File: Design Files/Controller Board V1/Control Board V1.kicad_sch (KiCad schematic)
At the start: 0 parts

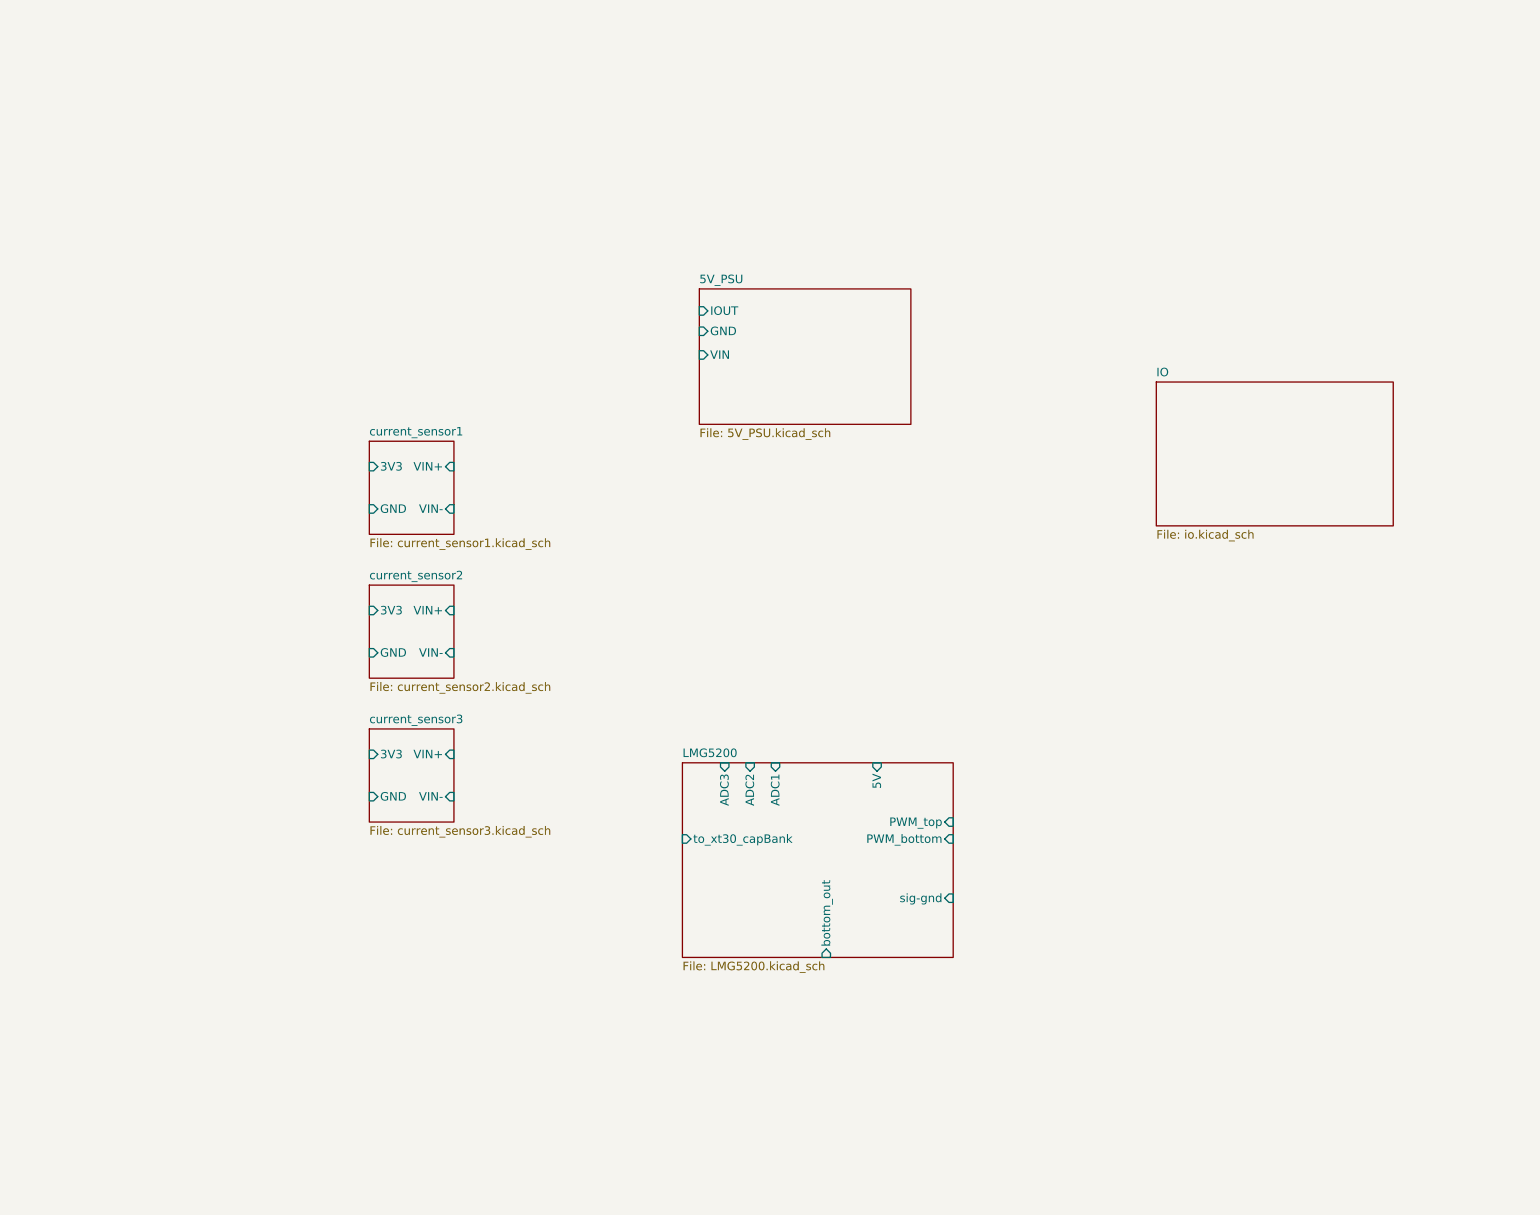
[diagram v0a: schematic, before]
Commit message: Pico Schematic Started
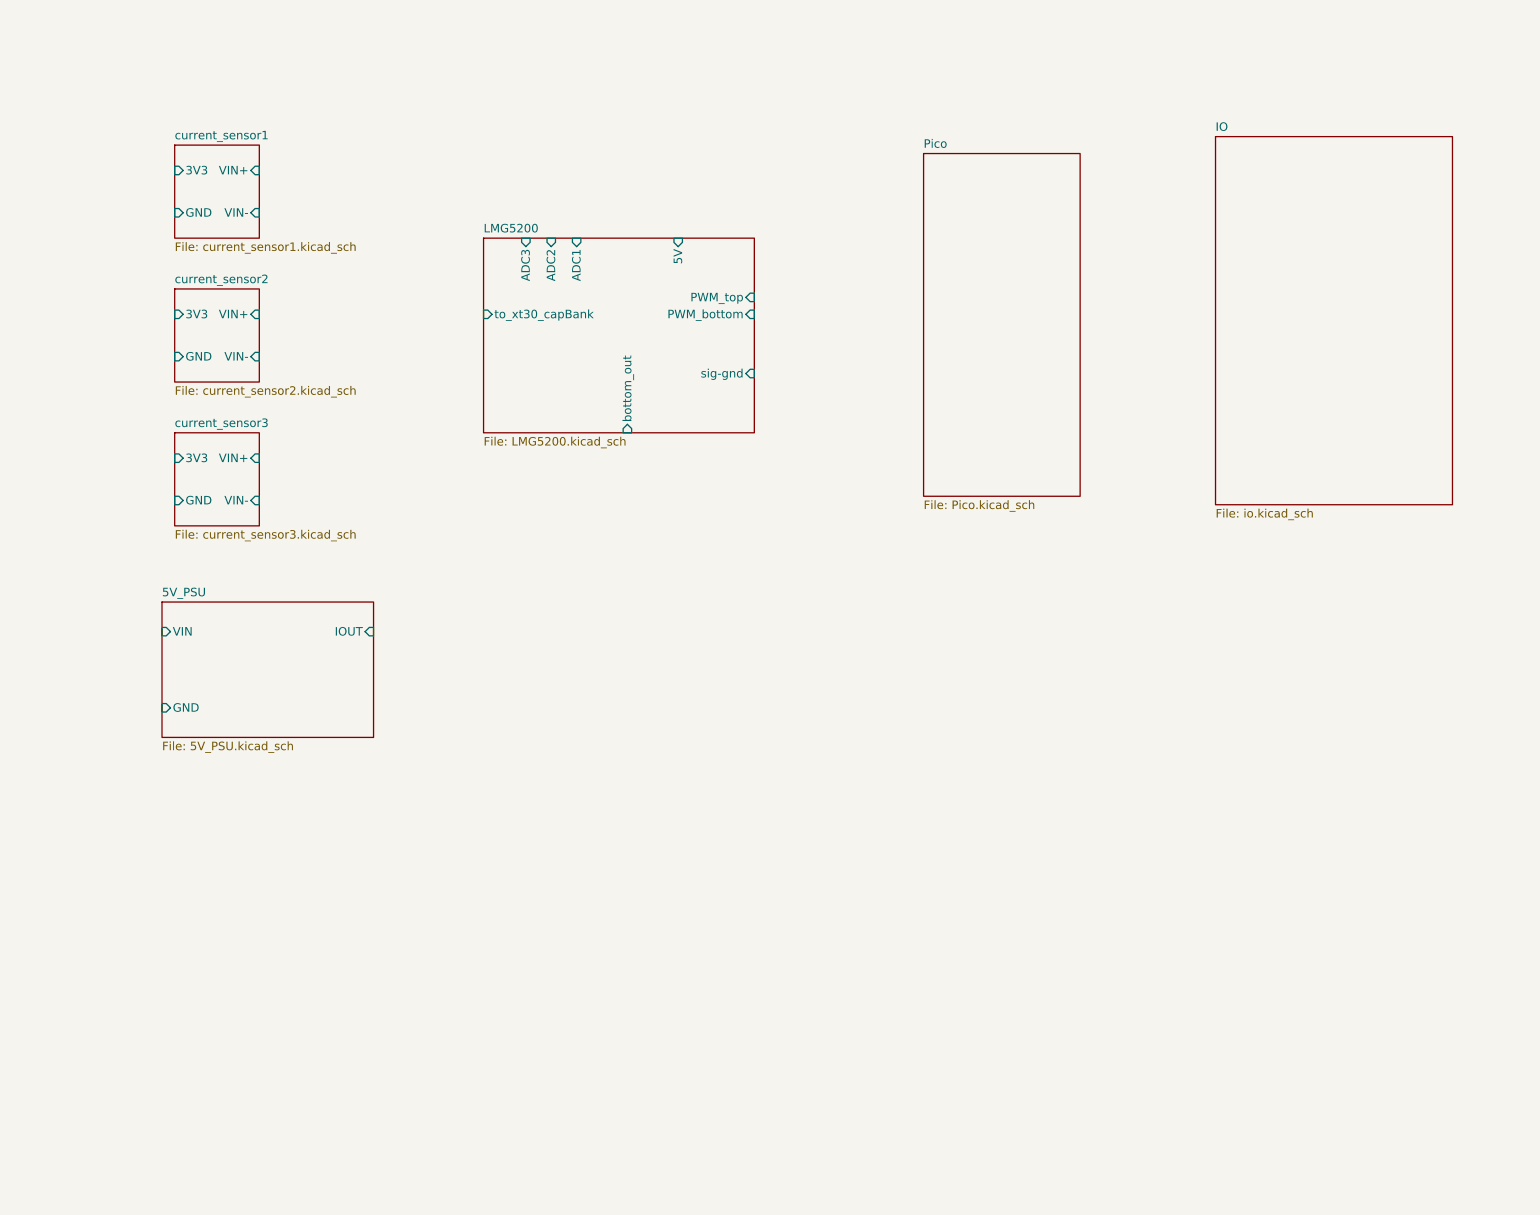
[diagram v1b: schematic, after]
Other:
- added sheet Pico (Pico.kicad_sch)
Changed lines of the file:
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@@
 	(paper "A4")
 	(sheet
-		(at 59.69 77.47)
+		(at 30.48 33.02)
 		(size 12.7 13.97)
 		(fields_autoplaced yes)
@@
 		)
 		(property "Sheetname" "current_sensor1"
-			(at 59.69 76.7584 0)
+			(at 30.48 32.3084 0)
 			(effects
 				(font
@@
 		)
 		(property "Sheetfile" "current_sensor1.kicad_sch"
-			(at 59.69 92.0246 0)
+			(at 30.48 47.5746 0)
 			(effects
 				(font
@@
 		)
 		(pin "3V3" input
-			(at 59.69 81.28 180)
+			(at 30.48 36.83 180)
 			(effects
 				(font
@@
 		)
 		(pin "GND" input
-			(at 59.69 87.63 180)
+			(at 30.48 43.18 180)
 			(effects
 				(font
@@
 		)
 		(pin "VIN+" input
-			(at 72.39 81.28 0)
+			(at 43.18 36.83 0)
 			(effects
 				(font
@@
 		)
 		(pin "VIN-" input
-			(at 72.39 87.63 0)
+			(at 43.18 43.18 0)
 			(effects
 				(font
@@
 	)
 	(sheet
-		(at 106.68 125.73)
+		(at 142.875 34.29)
+		(size 23.495 51.435)
+		(fields_autoplaced yes)
+		(stroke
+			(width 0.1524)
+			(type solid)
+		)
+		(fill
+			(color 0 0 0 0.0000)
+		)
+		(property "Sheetname" "Pico"
+			(at 142.875 33.5784 0)
+			(effects
+				(font
+					(size 1.27 1.27)
+				)
+				(justify left bottom)
+			)
+		)
+		(property "Sheetfile" "Pico.kicad_sch"
+			(at 142.875 86.3096 0)
+			(effects
+				(font
+					(size 1.27 1.27)
+				)
+				(justify left top)
+			)
+		)
+		(instances
+			(project "Control Board V1"
+				(path "/e0c606b8-cbb9-4aff-b96c-73876da6ca74"
+					(page "8")
+				)
+			)
+		)
+	)
+	(sheet
+		(at 76.835 46.99)
 		(size 40.64 29.21)
 		(fields_autoplaced yes)
@@
 		)
 		(property "Sheetname" "LMG5200"
-			(at 106.68 125.0184 0)
+			(at 76.835 46.2784 0)
 			(effects
 				(font
@@
 		)
 		(property "Sheetfile" "LMG5200.kicad_sch"
-			(at 106.68 155.5246 0)
+			(at 76.835 76.7846 0)
 			(effects
 				(font
@@
 		)
 		(pin "sig-gnd" input
-			(at 147.32 146.05 0)
+			(at 117.475 67.31 0)
 			(effects
 				(font
@@
 		)
 		(pin "5V" input
-			(at 135.89 125.73 90)
+			(at 106.045 46.99 90)
 			(effects
 				(font
@@
 		)
 		(pin "bottom_out" input
-			(at 128.27 154.94 270)
+			(at 98.425 76.2 270)
 			(effects
 				(font
@@
 		)
 		(pin "to_xt30_capBank" input
-			(at 106.68 137.16 180)
+			(at 76.835 58.42 180)
 			(effects
 				(font
@@
 		)
 		(pin "ADC3" input
-			(at 113.03 125.73 90)
+			(at 83.185 46.99 90)
 			(effects
 				(font
@@
 		)
 		(pin "ADC2" input
-			(at 116.84 125.73 90)
+			(at 86.995 46.99 90)
 			(effects
 				(font
@@
 		)
 		(pin "PWM_top" input
-			(at 147.32 134.62 0)
+			(at 117.475 55.88 0)
 			(effects
 				(font
@@
 		)
 		(pin "PWM_bottom" input
-			(at 147.32 137.16 0)
+			(at 117.475 58.42 0)
 			(effects
 				(font
@@
 		)
 		(pin "ADC1" input
-			(at 120.65 125.73 90)
+			(at 90.805 46.99 90)
 			(effects
 				(font
@@
 	)
 	(sheet
-		(at 177.8 68.58)
-		(size 35.56 21.59)
+		(at 186.69 31.75)
+		(size 35.56 55.245)
 		(fields_autoplaced yes)
 		(stroke
@@
 		)
 		(property "Sheetname" "IO"
-			(at 177.8 67.8684 0)
+			(at 186.69 31.0384 0)
 			(effects
 				(font
@@
 		)
 		(property "Sheetfile" "io.kicad_sch"
-			(at 177.8 90.7546 0)
+			(at 186.69 87.5796 0)
 			(effects
 				(font
@@
 	)
 	(sheet
-		(at 59.69 99.06)
+		(at 30.48 54.61)
 		(size 12.7 13.97)
 		(fields_autoplaced yes)
@@
 		)
 		(property "Sheetname" "current_sensor2"
-			(at 59.69 98.3484 0)
+			(at 30.48 53.8984 0)
 			(effects
 				(font
@@
 		)
 		(property "Sheetfile" "current_sensor2.kicad_sch"
-			(at 59.69 113.6146 0)
+			(at 30.48 69.1646 0)
 			(effects
 				(font
@@
 		)
 		(pin "3V3" input
-			(at 59.69 102.87 180)
+			(at 30.48 58.42 180)
 			(effects
 				(font
@@
 		)
 		(pin "VIN+" input
-			(at 72.39 102.87 0)
+			(at 43.18 58.42 0)
 			(effects
 				(font
@@
 		)
 		(pin "VIN-" input
-			(at 72.39 109.22 0)
+			(at 43.18 64.77 0)
 			(effects
 				(font
@@
 		)
 		(pin "GND" input
-			(at 59.69 109.22 180)
+			(at 30.48 64.77 180)
 			(effects
 				(font
@@
 	)
 	(sheet
-		(at 109.22 54.61)
+		(at 28.575 101.6)
 		(size 31.75 20.32)
 		(fields_autoplaced yes)
@@
 		)
 		(property "Sheetname" "5V_PSU"
-			(at 109.22 53.8984 0)
+			(at 28.575 100.8884 0)
 			(effects
 				(font
@@
 		)
 		(property "Sheetfile" "5V_PSU.kicad_sch"
-			(at 109.22 75.5146 0)
+			(at 28.575 122.5046 0)
 			(effects
 				(font
@@
 		)
 		(pin "IOUT" input
-			(at 109.22 57.912 180)
-			(effects
-				(font
-					(size 1.27 1.27)
-				)
-				(justify left)
+			(at 60.325 106.045 0)
+			(effects
+				(font
+					(size 1.27 1.27)
+				)
+				(justify right)
 			)
 		)
 		(pin "GND" input
-			(at 109.22 60.96 180)
+			(at 28.575 117.475 180)
 			(effects
 				(font
@@
 		)
 		(pin "VIN" input
-			(at 109.22 64.516 180)
+			(at 28.575 106.045 180)
 			(effects
 				(font
@@
 	)
 	(sheet
-		(at 59.69 120.65)
+		(at 30.48 76.2)
 		(size 12.7 13.97)
 		(fields_autoplaced yes)
@@
 		)
 		(property "Sheetname" "current_sensor3"
-			(at 59.69 119.9384 0)
+			(at 30.48 75.4884 0)
 			(effects
 				(font
@@
 		)
 		(property "Sheetfile" "current_sensor3.kicad_sch"
-			(at 59.69 135.2046 0)
+			(at 30.48 90.7546 0)
 			(effects
 				(font
@@
 		)
 		(pin "GND" input
-			(at 59.69 130.81 180)
+			(at 30.48 86.36 180)
 			(effects
 				(font
@@
 		)
 		(pin "3V3" input
-			(at 59.69 124.46 180)
+			(at 30.48 80.01 180)
 			(effects
 				(font
@@
 		)
 		(pin "VIN-" input
-			(at 72.39 130.81 0)
+			(at 43.18 86.36 0)
 			(effects
 				(font
@@
 		)
 		(pin "VIN+" input
-			(at 72.39 124.46 0)
-			(effects
-				(font
+			(at 43.18 80.01 0)
+			(effects
+				(font

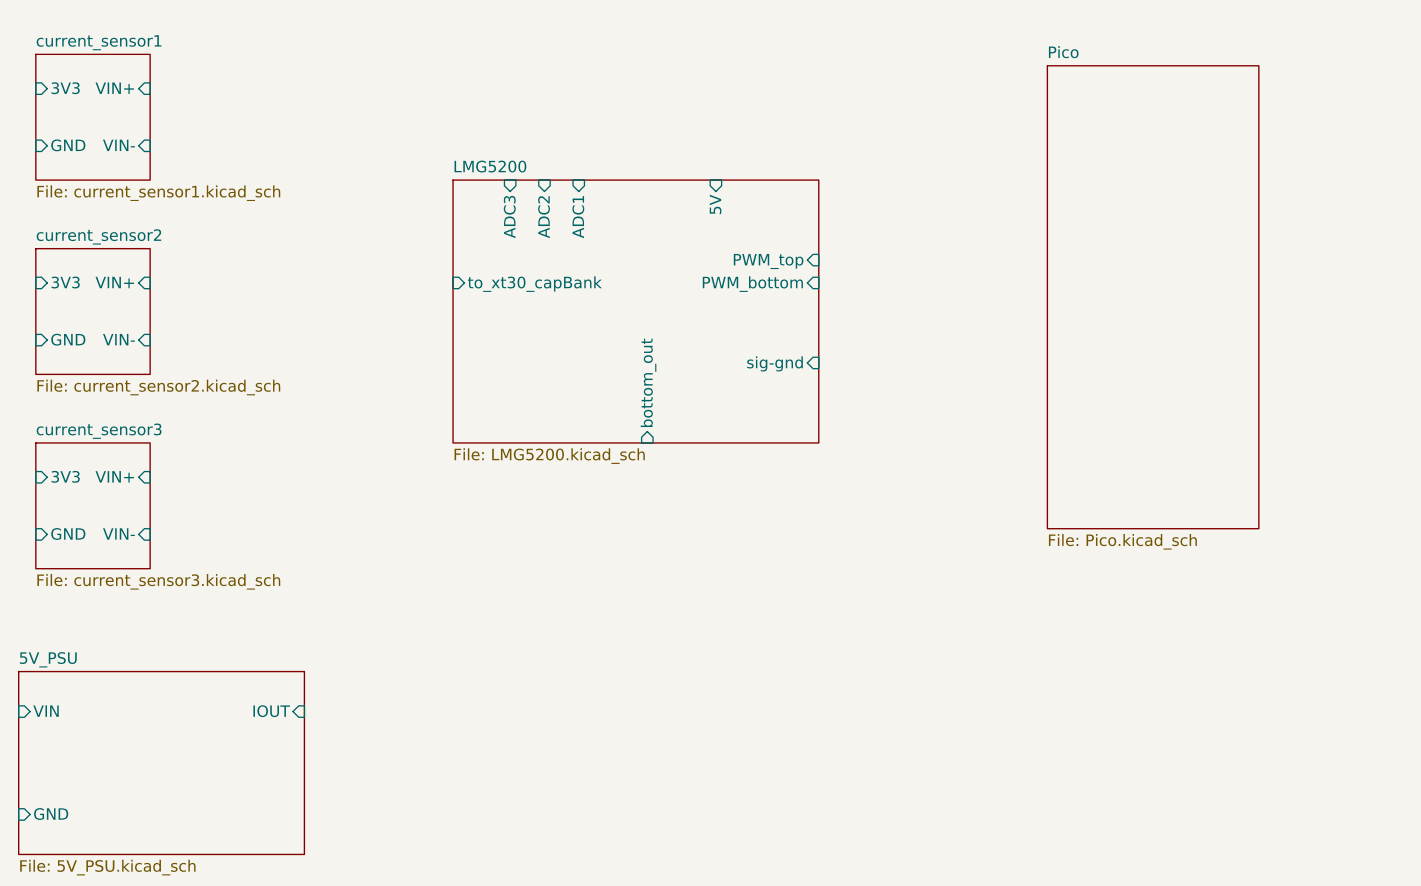
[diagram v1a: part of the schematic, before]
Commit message: I2C channels for pico and current sensors
gaming B)
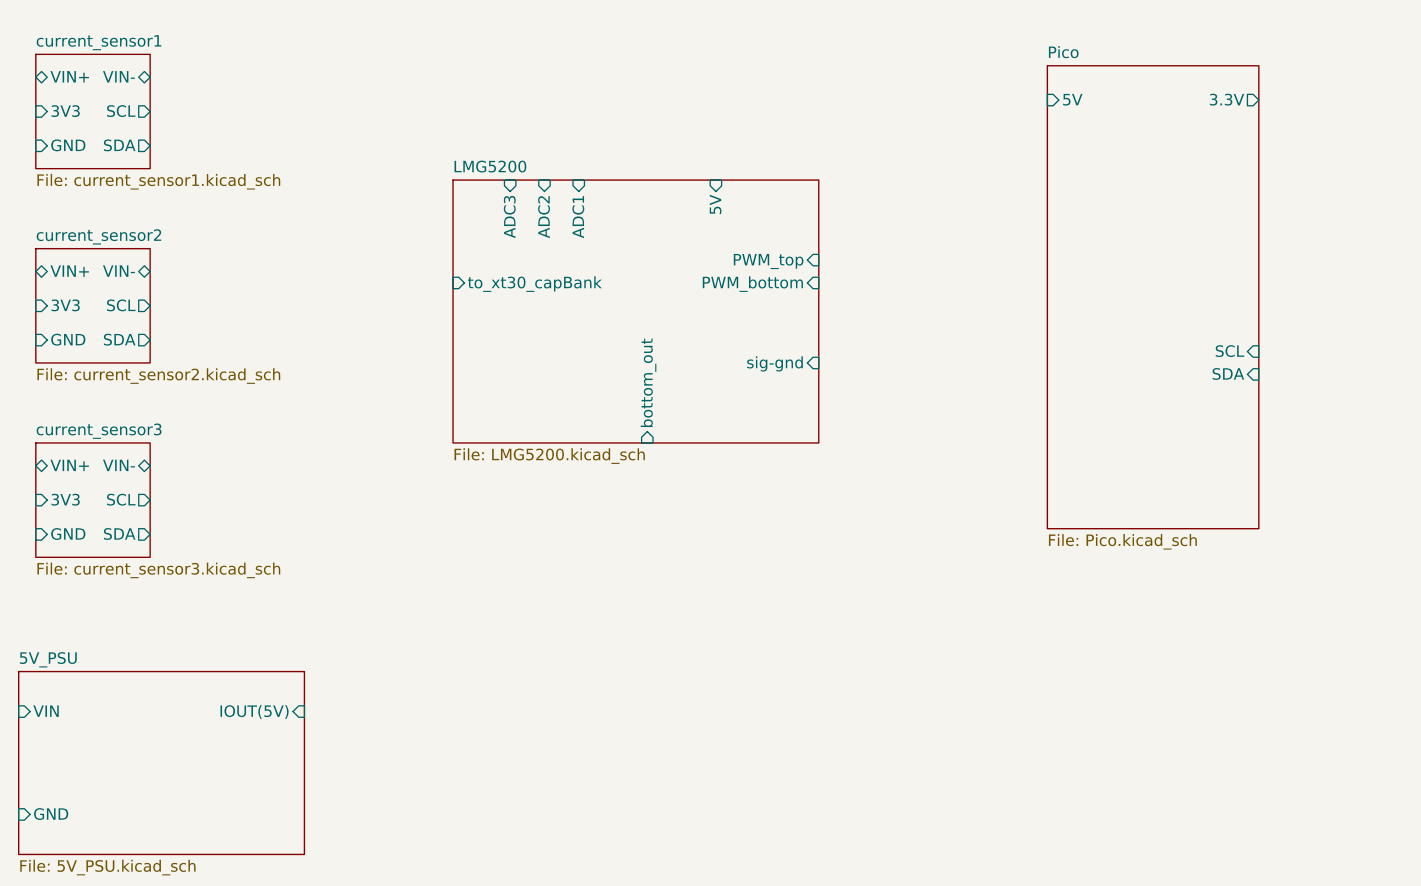
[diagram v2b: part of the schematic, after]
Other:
- sheet 5V_PSU ports: added IOUT(5V); removed IOUT
- sheet Pico ports: added 3.3V, 5V, SCL, SDA; removed none
- sheet current_sensor1 ports: added SCL, SDA; removed none
- sheet current_sensor2 ports: added SCL, SDA; removed none
- sheet current_sensor3 ports: added SCL, SDA; removed none
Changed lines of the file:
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@@
 	(sheet
 		(at 30.48 33.02)
-		(size 12.7 13.97)
+		(size 12.7 12.7)
 		(fields_autoplaced yes)
 		(stroke
@@
 		)
 		(property "Sheetfile" "current_sensor1.kicad_sch"
-			(at 30.48 47.5746 0)
+			(at 30.48 46.3046 0)
 			(effects
 				(font
@@
 		)
 		(pin "3V3" input
-			(at 30.48 36.83 180)
+			(at 30.48 39.37 180)
 			(effects
 				(font
@@
 			)
 		)
-		(pin "VIN+" input
-			(at 43.18 36.83 0)
-			(effects
-				(font
-					(size 1.27 1.27)
-				)
-				(justify right)
-			)
-		)
-		(pin "VIN-" input
+		(pin "VIN+" bidirectional
+			(at 30.48 35.56 180)
+			(effects
+				(font
+					(size 1.27 1.27)
+				)
+				(justify left)
+			)
+		)
+		(pin "VIN-" bidirectional
+			(at 43.18 35.56 0)
+			(effects
+				(font
+					(size 1.27 1.27)
+				)
+				(justify right)
+			)
+		)
+		(pin "SCL" output
+			(at 43.18 39.37 0)
+			(effects
+				(font
+					(size 1.27 1.27)
+				)
+				(justify right)
+			)
+		)
+		(pin "SDA" output
 			(at 43.18 43.18 0)
 			(effects
@@
 			)
 		)
+		(pin "3.3V" output
+			(at 166.37 38.1 0)
+			(effects
+				(font
+					(size 1.27 1.27)
+				)
+				(justify right)
+			)
+		)
+		(pin "5V" input
+			(at 142.875 38.1 180)
+			(effects
+				(font
+					(size 1.27 1.27)
+				)
+				(justify left)
+			)
+		)
+		(pin "SCL" input
+			(at 166.37 66.04 0)
+			(effects
+				(font
+					(size 1.27 1.27)
+				)
+				(justify right)
+			)
+		)
+		(pin "SDA" input
+			(at 166.37 68.58 0)
+			(effects
+				(font
+					(size 1.27 1.27)
+				)
+				(justify right)
+			)
+		)
 		(instances
 			(project "Control Board V1"
@@
 	(sheet
 		(at 30.48 54.61)
-		(size 12.7 13.97)
+		(size 12.7 12.7)
 		(fields_autoplaced yes)
 		(stroke
@@
 		)
 		(property "Sheetfile" "current_sensor2.kicad_sch"
-			(at 30.48 69.1646 0)
+			(at 30.48 67.8946 0)
 			(effects
 				(font
@@
 		)
 		(pin "3V3" input
-			(at 30.48 58.42 180)
-			(effects
-				(font
-					(size 1.27 1.27)
-				)
-				(justify left)
-			)
-		)
-		(pin "VIN+" input
-			(at 43.18 58.42 0)
-			(effects
-				(font
-					(size 1.27 1.27)
-				)
-				(justify right)
-			)
-		)
-		(pin "VIN-" input
-			(at 43.18 64.77 0)
+			(at 30.48 60.96 180)
+			(effects
+				(font
+					(size 1.27 1.27)
+				)
+				(justify left)
+			)
+		)
+		(pin "VIN+" bidirectional
+			(at 30.48 57.15 180)
+			(effects
+				(font
+					(size 1.27 1.27)
+				)
+				(justify left)
+			)
+		)
+		(pin "VIN-" bidirectional
+			(at 43.18 57.15 0)
 			(effects
 				(font
@@
 				)
 				(justify left)
+			)
+		)
+		(pin "SCL" output
+			(at 43.18 60.96 0)
+			(effects
+				(font
+					(size 1.27 1.27)
+				)
+				(justify right)
+			)
+		)
+		(pin "SDA" output
+			(at 43.18 64.77 0)
+			(effects
+				(font
+					(size 1.27 1.27)
+				)
+				(justify right)
 			)
 		)
@@
 			)
 		)
-		(pin "IOUT" input
+		(pin "IOUT(5V)" input
 			(at 60.325 106.045 0)
 			(effects
@@
 	(sheet
 		(at 30.48 76.2)
-		(size 12.7 13.97)
+		(size 12.7 12.7)
 		(fields_autoplaced yes)
 		(stroke
@@
 		)
 		(property "Sheetfile" "current_sensor3.kicad_sch"
-			(at 30.48 90.7546 0)
+			(at 30.48 89.4846 0)
 			(effects
 				(font
@@
 		)
 		(pin "3V3" input
-			(at 30.48 80.01 180)
-			(effects
-				(font
-					(size 1.27 1.27)
-				)
-				(justify left)
-			)
-		)
-		(pin "VIN-" input
+			(at 30.48 82.55 180)
+			(effects
+				(font
+					(size 1.27 1.27)
+				)
+				(justify left)
+			)
+		)
+		(pin "VIN-" bidirectional
+			(at 43.18 78.74 0)
+			(effects
+				(font
+					(size 1.27 1.27)
+				)
+				(justify right)
+			)
+		)
+		(pin "VIN+" bidirectional
+			(at 30.48 78.74 180)
+			(effects
+				(font
+					(size 1.27 1.27)
+				)
+				(justify left)
+			)
+		)
+		(pin "SCL" output
+			(at 43.18 82.55 0)
+			(effects
+				(font
+					(size 1.27 1.27)
+				)
+				(justify right)
+			)
+		)
+		(pin "SDA" output
 			(at 43.18 86.36 0)
 			(effects
 				(font
-					(size 1.27 1.27)
-				)
-				(justify right)
-			)
-		)
-		(pin "VIN+" input
-			(at 43.18 80.01 0)
-			(effects
-				(font
